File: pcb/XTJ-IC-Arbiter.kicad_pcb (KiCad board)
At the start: 2 copper layers, 82.4 x 56.2 mm, 33 parts, among them J3 DTM13-12PA-R008, SW2 SW_DIP_x02, U1 LM2672N-5.0, U3 Teensy4.0, U4 MCP2562-H-P, U5 SP723ABG

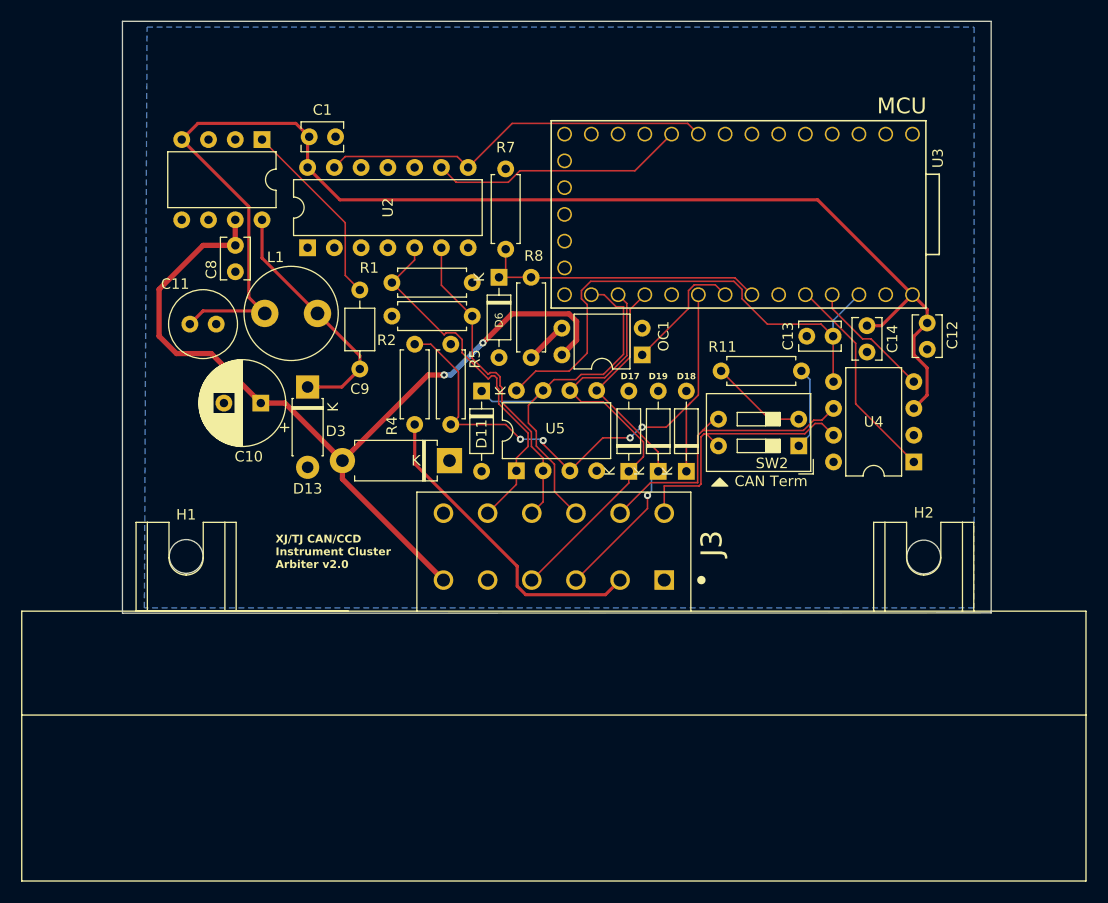
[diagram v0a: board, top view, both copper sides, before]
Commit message: tune can termination length
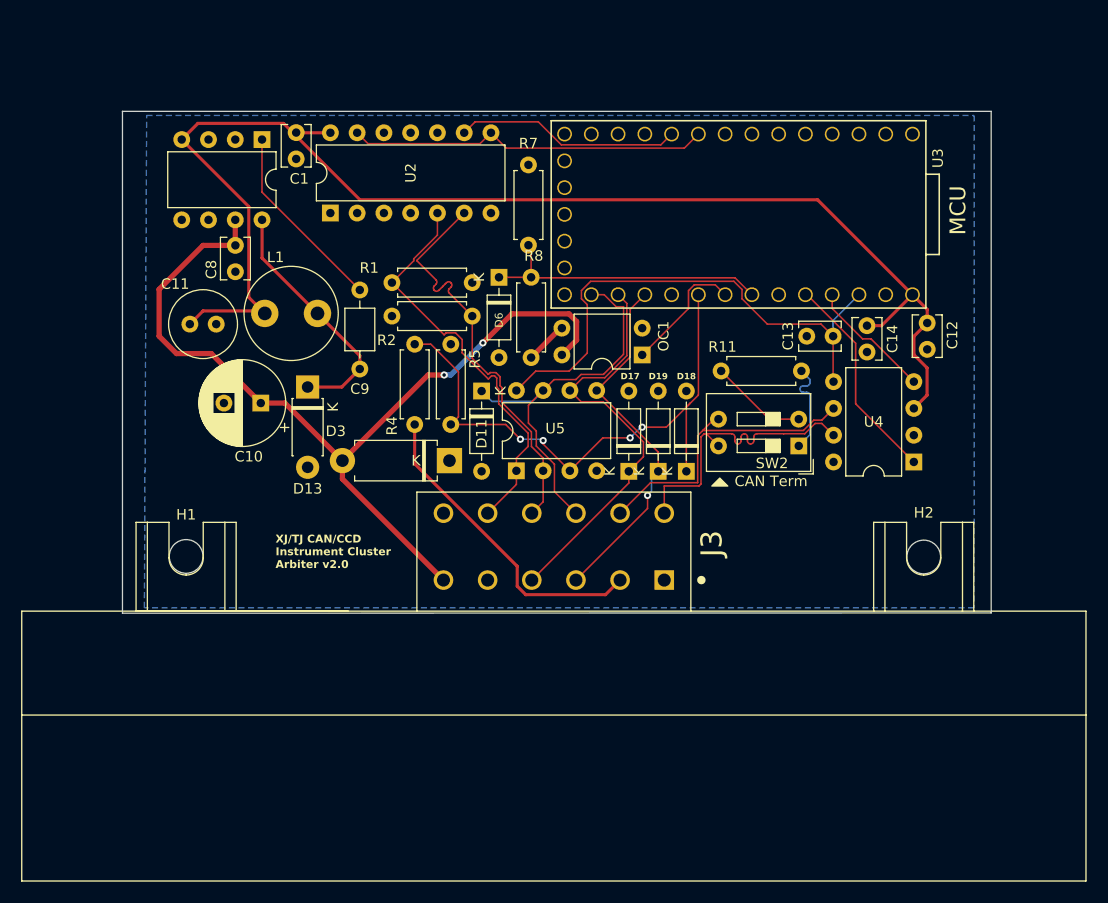
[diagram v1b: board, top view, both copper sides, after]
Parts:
- moved U2 3.94 mm to (70.0, 97.7)
- moved R7 2.19 mm to (88.8, 100.7)
- moved C1 1.30 mm to (66.7, 90.0), turned to -90 degrees
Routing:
- net ccd-: track 30.3 -> 38.8 mm
- net ccd+: track 34.7 -> 38.9 mm
- net rxd: track 37.6 -> 34.4 mm
- net txd: track 24.3 -> 21.4 mm
- net can+: track 26.0 -> 28.8 mm
- net +5V: track 124.0 -> 125.9 mm
- net Net-(R11-Pad2): track 7.88 -> 9.20 mm
- net 12V_MEASURE: track 26.6 -> 27.8 mm
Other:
- board size 82.4 x 56.2 mm -> 82.4 x 47.6 mm

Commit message: fix board edge
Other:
- board size 82.4 x 47.6 mm -> 82.1 x 48.1 mm
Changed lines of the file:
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@@
     )
     (stroke (width 0.12) (type solid)) (fill solid) (layer "F.SilkS"))
-  (gr_line (start 50.24 88.011) (end 132.69 88.011)
-    (stroke (width 0.05) (type default)) (layer "Edge.Cuts"))
-  (gr_line (start 50.244 135.64) (end 50.244 88.008)
-    (stroke (width 0.05) (type solid)) (layer "Edge.Cuts"))
-  (gr_line (start 132.69 88.011) (end 132.69 135.61)
-    (stroke (width 0.05) (type solid)) (layer "Edge.Cuts"))
-  (gr_line (start 132.69 135.61) (end 50.244 135.64)
-    (stroke (width 0.05) (type solid)) (layer "Edge.Cuts"))
+  (gr_rect (start 50.39 87.238) (end 132.51 135.338)
+    (stroke (width 0.05) (type default)) (fill none) (layer "Edge.Cuts"))
   (gr_text "CCD-\n" (at 88.6968 123.952) (layer "B.SilkS")
     (effects (font (size 1 1) (thickness 0.15)) (justify mirror))

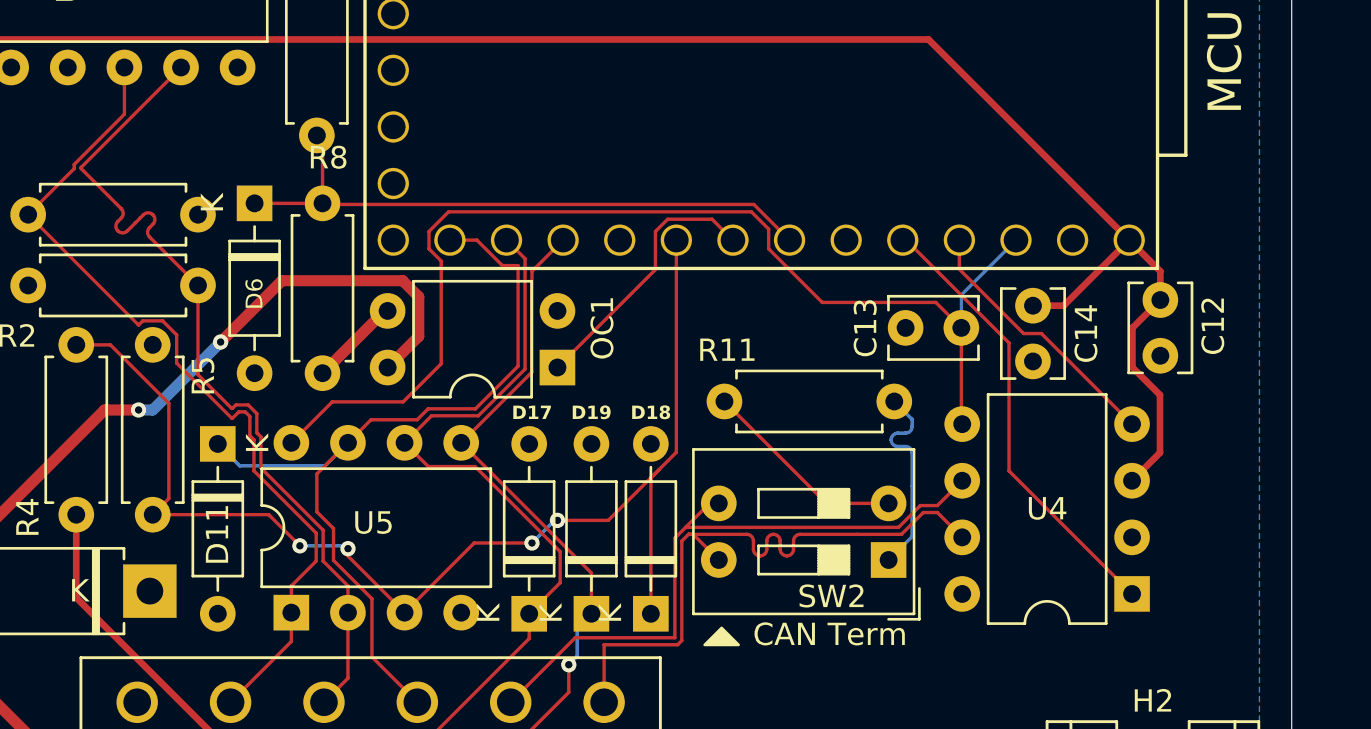
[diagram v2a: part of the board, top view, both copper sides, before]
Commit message: cleanup bypass caps
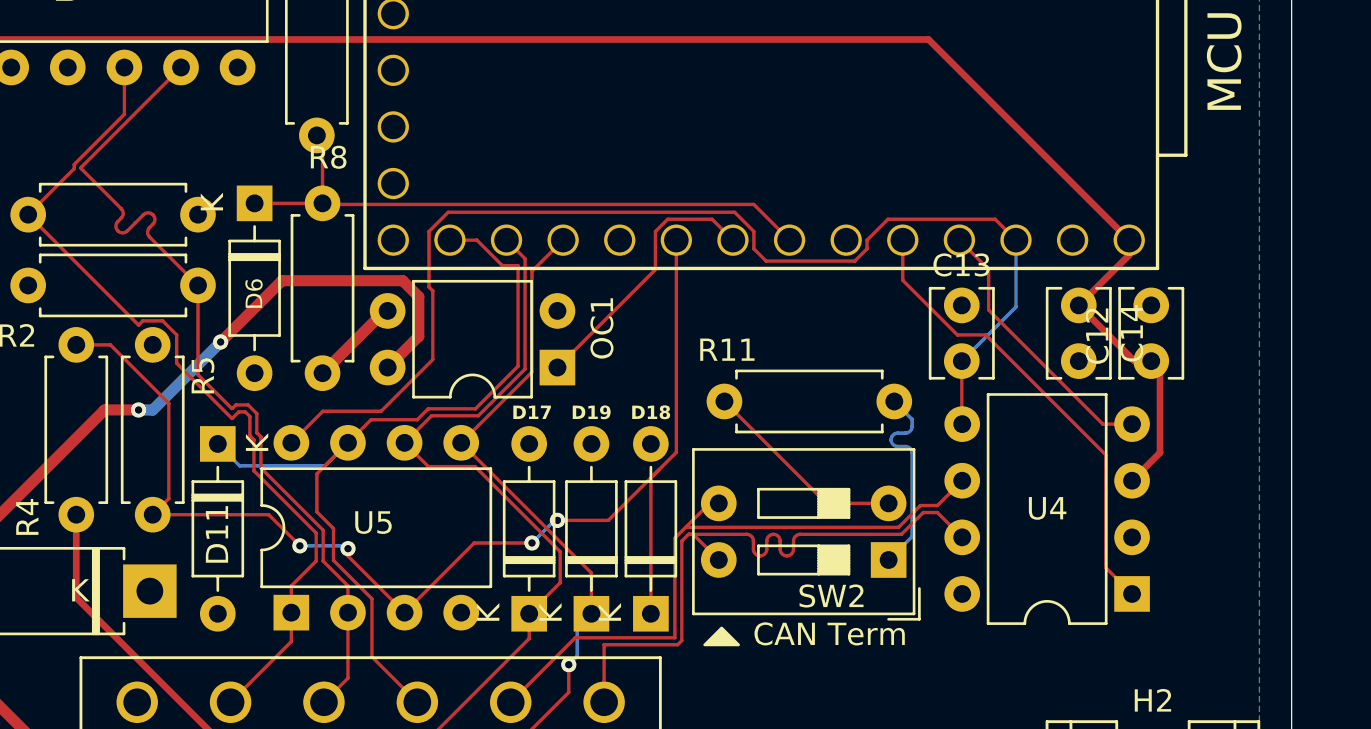
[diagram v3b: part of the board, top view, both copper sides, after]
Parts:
- moved C12 2.30 mm to (126.2, 108.3), turned to -90 degrees
- moved C14 2.06 mm to (123.0, 108.3)
- moved C13 1.49 mm to (117.7, 110.8), turned to 90 degrees
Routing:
- net +5V: track 125.9 -> 121.1 mm
- net 3v3: track 50.5 -> 52.4 mm
- net can_tx: track 20.1 -> 20.9 mm

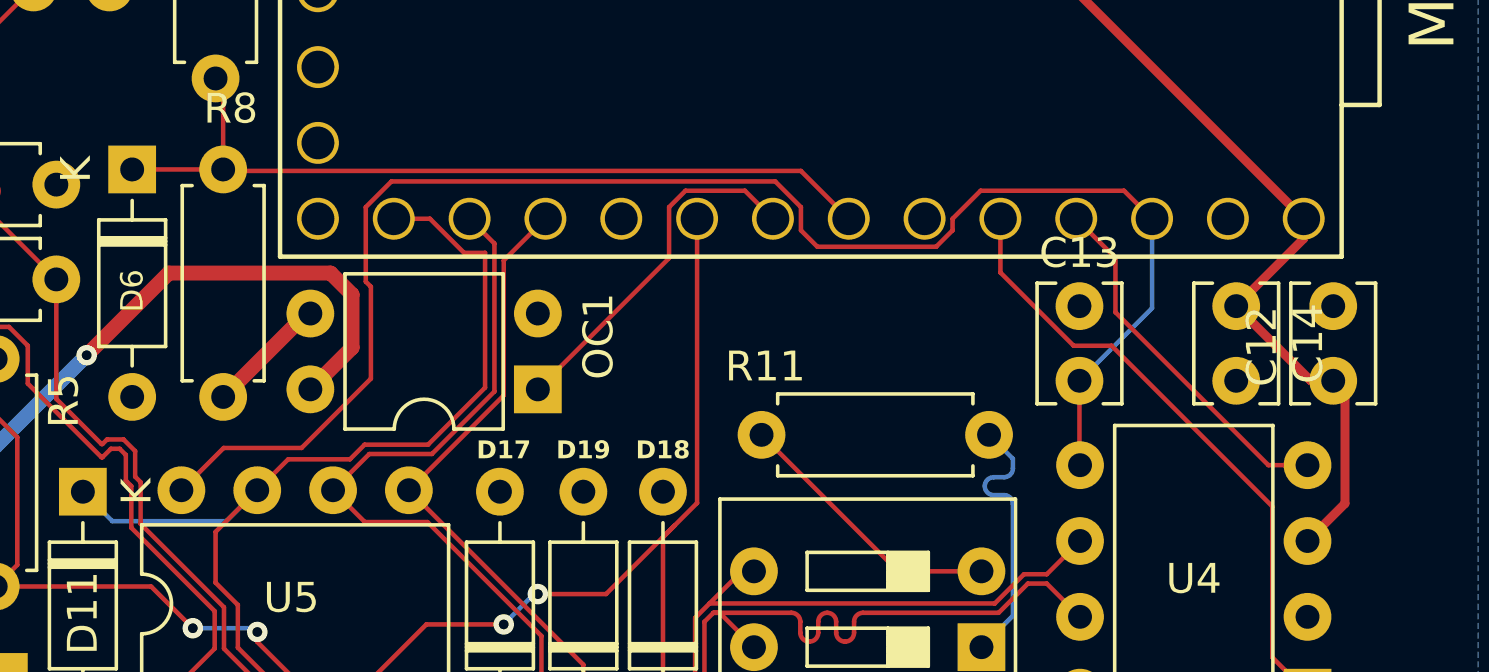
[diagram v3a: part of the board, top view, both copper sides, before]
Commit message: get rid of 5v feed text
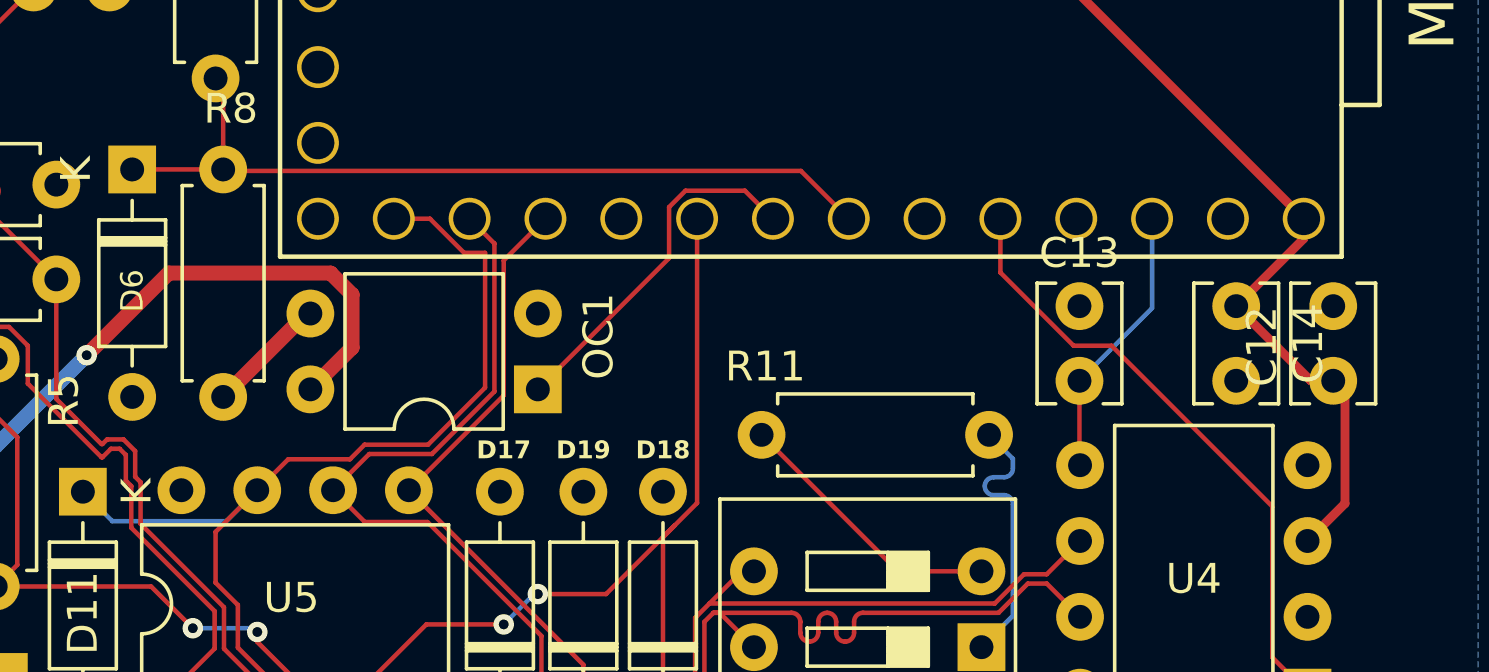
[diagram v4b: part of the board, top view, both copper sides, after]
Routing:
- net 3v3: track 52.4 -> 9.27 mm
- net can_rx: track 12.2 -> 0.00 mm
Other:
- board text removed: "+5V"
- board text removed: "250mA Max +5V External Load"
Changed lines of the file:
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@@
     )
   )
-  (gr_line (start 83.439 129.54) (end 83.439 129.032)
-    (stroke (width 0.12) (type solid)) (layer "B.SilkS"))
   (gr_poly
     (pts
@@
     )
     (stroke (width 0.04) (type solid)) (fill solid) (layer "B.SilkS"))
-  (gr_line (start 78.359 128.778) (end 82.677 128.778)
-    (stroke (width 0.12) (type solid)) (layer "B.SilkS"))
   (gr_poly
     (pts
@@
     )
     (stroke (width 0.04) (type solid)) (fill solid) (layer "B.SilkS"))
-  (gr_line (start 83.439 129.54) (end 82.677 128.778)
-    (stroke (width 0.12) (type solid)) (layer "B.SilkS"))
-  (gr_line (start 82.931 129.54) (end 83.439 129.54)
-    (stroke (width 0.12) (type solid)) (layer "B.SilkS"))
-  (gr_line (start 83.439 129.54) (end 82.931 129.54)
-    (stroke (width 0.12) (type solid)) (layer "B.SilkS"))
   (gr_poly
     (pts
@@
     (effects (font (size 1.5 1.5) (thickness 0.3)) (justify mirror))
   )
-  (gr_text "+5V" (at 85.09 130.302) (layer "B.SilkS")
-    (effects (font (size 0.75 0.75) (thickness 0.15)) (justify mirror))
-  )
   (gr_text "IO/2" (at 88.9 130.175) (layer "B.SilkS")
     (effects (font (size 1 1) (thickness 0.15)) (justify mirror))
@@
   )
   (gr_text "GND" (at 80.772 123.952) (layer "B.SilkS")
-    (effects (font (size 1 1) (thickness 0.15)) (justify mirror))
-  )
-  (gr_text "250mA Max +5V \nExternal Load" (at 72.009 128.143) (layer "B.SilkS")
     (effects (font (size 1 1) (thickness 0.15)) (justify mirror))
   )
@@
   (segment (start 115.062 107.211977) (end 115.062 105.41) (width 0.1524) (layer "F.Cu") (net 8))
   (segment (start 124.168 120.104) (end 124.168 115.046) (width 0.1524) (layer "F.Cu") (net 8))
-  (segment (start 124.037 113.665) (end 125.349 113.665) (width 0.1524) (layer "F.Cu") (net 9))
-  (segment (start 118.9156 106.7236) (end 118.9156 108.5436) (width 0.1524) (layer "F.Cu") (net 9))
-  (segment (start 117.602 105.41) (end 118.9156 106.7236) (width 0.1524) (layer "F.Cu") (net 9))
-  (segment (start 118.9156 108.5436) (end 124.037 113.665) (width 0.1524) (layer "F.Cu") (net 9))
   (segment (start 63.49 90.688) (end 63.49 95.681) (width 0.1524) (layer "F.Cu") (net 10))
   (segment (start 63.49 95.681) (end 72.771 104.962) (width 0.1524) (layer "F.Cu") (net 10))
@@
   (segment (start 103.9638 106.7292) (end 103.9638 105.021384) (width 0.1524) (layer "F.Cu") (net 17))
   (segment (start 91.821 108.585) (end 89.027 111.379) (width 0.5) (layer "F.Cu") (net 18))
-  (segment (start 119.2038 104.4718) (end 114.3984 104.4718) (width 0.1524) (layer "F.Cu") (net 20))
-  (segment (start 93.976 107.688631) (end 93.976 110.767187) (width 0.1524) (layer "F.Cu") (net 20))
-  (segment (start 112.910616 106.3482) (end 108.929784 106.3482) (width 0.1524) (layer "F.Cu") (net 20))
-  (segment (start 107.518216 104.1594) (end 94.665784 104.1594) (width 0.1524) (layer "F.Cu") (net 20))
-  (segment (start 113.4602 105.798616) (end 112.910616 106.3482) (width 0.1524) (layer "F.Cu") (net 20))
-  (segment (start 108.929784 106.3482) (end 108.3802 105.798616) (width 0.1524) (layer "F.Cu") (net 20))
-  (segment (start 113.4602 105.41) (end 113.4602 105.798616) (width 0.1524) (layer "F.Cu") (net 20))
   (segment (start 117.71 113.646) (end 117.729 113.665) (width 0.1524) (layer "F.Cu") (net 20))
-  (segment (start 108.3802 105.021384) (end 107.518216 104.1594) (width 0.1524) (layer "F.Cu") (net 20))
-  (segment (start 108.3802 105.798616) (end 108.3802 105.021384) (width 0.1524) (layer "F.Cu") (net 20))
-  (segment (start 94.665784 104.1594) (end 93.8038 105.021384) (width 0.1524) (layer "F.Cu") (net 20))
-  (segment (start 91.655187 113.088) (end 89.044 113.088) (width 0.1524) (layer "F.Cu") (net 20))
-  (segment (start 120.142 105.41) (end 119.2038 104.4718) (width 0.1524) (layer "F.Cu") (net 20))
-  (segment (start 114.3984 104.4718) (end 113.4602 105.41) (width 0.1524) (layer "F.Cu") (net 20))
-  (segment (start 93.8038 105.021384) (end 93.8038 107.516431) (width 0.1524) (layer "F.Cu") (net 20))
-  (segment (start 93.8038 107.516431) (end 93.976 107.688631) (width 0.1524) (layer "F.Cu") (net 20))
-  (segment (start 89.044 113.088) (end 87.628 114.504) (width 0.1524) (layer "F.Cu") (net 20))
-  (segment (start 93.976 110.767187) (end 91.655187 113.088) (width 0.1524) (layer "F.Cu") (net 20))
   (segment (start 117.71 110.838) (end 117.71 113.646) (width 0.1524) (layer "F.Cu") (net 20))
   (segment (start 120.142 108.406) (end 120.142 105.41) (width 0.1524) (layer "B.Cu") (net 20))

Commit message: convert unused pin to gnd
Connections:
- J3 pad 5: unconnected-(J3-Pad5) -> GND
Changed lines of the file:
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@@
   (net 44 "ctrl")
   (net 45 "rxd")
-  (net 46 "unconnected-(J3-Pad5)")
-  (net 47 "unconnected-(R1-Pad1)")
+  (net 46 "unconnected-(R1-Pad1)")
   (footprint "Capacitor_THT:C_Disc_D3.8mm_W2.6mm_P2.50mm" (layer "F.Cu")
     (at 117.71 110.838 90)
@@
       (net 12 "IO{slash}2") (pinfunction "4") (pintype "passive"))
     (pad "5" thru_hole circle (at -6.285 1.96) (size 1.86 1.86) (drill 1.24) (layers "*.Cu" "*.Mask")
-      (net 46 "unconnected-(J3-Pad5)") (pinfunction "5") (pintype "passive+no_connect"))
+      (net 19 "GND") (pinfunction "5") (pintype "passive"))
     (pad "6" thru_hole circle (at -10.475 1.96) (size 1.86 1.86) (drill 1.24) (layers "*.Cu" "*.Mask")
       (net 15 "+12V") (pinfunction "6") (pintype "passive"))
@@
       (stroke (width 0.1) (type solid)) (layer "F.Fab"))
     (pad "1" thru_hole circle (at 0 0 180) (size 1.6 1.6) (drill 0.8) (layers "*.Cu" "*.Mask")
-      (net 47 "unconnected-(R1-Pad1)") (pintype "passive"))
+      (net 46 "unconnected-(R1-Pad1)") (pintype "passive"))
     (pad "2" thru_hole oval (at 7.62 0 180) (size 1.6 1.6) (drill 0.8) (layers "*.Cu" "*.Mask")
       (net 2 "ccd+") (pintype "passive"))
@@
     (effects (font (size 1 1) (thickness 0.15)) (justify mirror))
   )
+  (gr_text "GND" (at 84.71 130.338) (layer "B.SilkS")
+    (effects (font (size 1 1) (thickness 0.15)) (justify mirror))
+  )
